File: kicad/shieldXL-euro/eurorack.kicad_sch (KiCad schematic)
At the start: 42 parts, among them J101 Eurorack power, J102 IN L, J103 IN R, J104 OUT L, J105 OUT R, J106 MIDI IN, J107 MIDI OUT, J108 USB-C 5V, J109 USB 1, J110 USB 2, J111 USB 3, J112 Pi USB 1, J113 Pi USB 2, J114 Pi USB 3, U101 TL074

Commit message: Corone schematic, and its jacks and header on the main board
kicad/corone: a generated schematic for the crow daughterboard, for monome's
own firmware - STM32F722RET6, ADS131A02 (symbol from TI's pin table), DAC8565,
OPA4197 output and input stages scaled to the firmware's conversions, ADG1408
calibration mux onto input 1's normal, switched ii pull-ups, USB with VBUS
sense, rack-only power. ERC: three expected warnings, no errors.

eurorack sheet: the six CORONE jacks (I/1's switch contact carried to the
mux), the 2 x 10 header, the ii header and a cable header for the Pi's
fourth USB port. Main-project ERC unchanged at 35.

Co-Authored-By: Claude Opus 5.5 <noreply@anthropic.com>
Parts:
- added J109: USB 1, Connector_USB:USB_A_Molex_105057_Vertical, symbol Connector:USB_A
- added J116: CORONE I/2, MMM:Jack_3.5mm_QingPu_WQP-PJ398SM_Vertical_CircularHoles, symbol Connector_Audio:AudioJack2_SwitchT
- added J117: CORONE O/1, MMM:Jack_3.5mm_QingPu_WQP-PJ398SM_Vertical_CircularHoles, symbol Connector_Audio:AudioJack2_SwitchT
- added J118: CORONE O/2, MMM:Jack_3.5mm_QingPu_WQP-PJ398SM_Vertical_CircularHoles, symbol Connector_Audio:AudioJack2_SwitchT
- added J119: CORONE O/3, MMM:Jack_3.5mm_QingPu_WQP-PJ398SM_Vertical_CircularHoles, symbol Connector_Audio:AudioJack2_SwitchT
- added J120: CORONE O/4, MMM:Jack_3.5mm_QingPu_WQP-PJ398SM_Vertical_CircularHoles, symbol Connector_Audio:AudioJack2_SwitchT
- added J121: Corone, Connector_PinHeader_2.54mm:PinHeader_2x10_P2.54mm_Vertical, symbol Connector_Generic:Conn_02x10_Odd_Even
- added J122: ii, Connector_PinHeader_2.54mm:PinHeader_1x03_P2.54mm_Vertical, symbol Connector_Generic:Conn_01x03
- added J123: Pi USB 4, Connector_JST:JST_PH_B4B-PH-K_1x04_P2.00mm_Vertical, symbol Connector_Generic:Conn_01x04
- J115: renamed from J109; value USB 1 -> CORONE I/1; footprint Connector_USB:USB_A_Molex_105057_Vertical -> MMM:Jack_3.5mm_QingPu_WQP-PJ398SM_Vertical_CircularHoles; symbol Connector:USB_A -> Connector_Audio:AudioJack2_SwitchT
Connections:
- net +12V: now also J121.1 (Pin_1)
- net -12V: now also J121.2 (Pin_2)
- net AGND: now also J115.S, J116.S, J116.TN, J117.S, J118.S, J119.S, J120.S, J121.13 (Pin_13), J121.14 (Pin_14), J121.18 (Pin_18), J121.3 (Pin_3), J121.4 (Pin_4), J121.8 (Pin_8), J122.1 (Pin_1)
- net GND: now also J109.4 (GND), J109.SH (Shield), J123.4 (Pin_4); no longer J115.4 (GND), J115.SH (Shield)
- net USB1_DM: now also J109.2 (D-); no longer J115.2 (D-)
- net USB1_DP: now also J109.3 (D+); no longer J115.3 (D+)
- net USB1_VBUS: now also J109.1 (VBUS); no longer J115.1 (VBUS)
- new net CRW_IN1: J115.T, J121.5 (Pin_5)
- new net CRW_IN1_NORM: J115.TN, J121.6 (Pin_6)
- new net CRW_IN2: J116.T, J121.7 (Pin_7)
- new net CRW_OUT1: J117.T, J121.9 (Pin_9)
- new net CRW_OUT2: J118.T, J121.10 (Pin_10)
- new net CRW_OUT3: J119.T, J121.11 (Pin_11)
- new net CRW_OUT4: J120.T, J121.12 (Pin_12)
- new net CRW_USB_DM: J121.16 (Pin_16), J123.2 (Pin_2)
- new net CRW_USB_DP: J121.15 (Pin_15), J123.3 (Pin_3)
- new net CRW_VBUS: J121.17 (Pin_17), J123.1 (Pin_1)
- new net II_SCL: J121.19 (Pin_19), J122.2 (Pin_2)
- new net II_SDA: J121.20 (Pin_20), J122.3 (Pin_3)
- no-connect marks 3 -> 7

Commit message: Pi USB adapter, and the main board's two IDC headers for it
kicad/usb-adapter: a generated board that stands at one of the Pi 4's USB
stacks, two vertical male USB-A plugs in its ports and a 2 x 5 IDC whose
ribbon runs behind the Pi to the main board; two identical boards cover the
four ports. The plug footprint and the port spacing are placeholders until
the part is chosen and the Pi measured. Unrouted.

eurorack sheet: J112 / J113, 2 x 5 IDC, replace the four JST cable headers;
Corone's USB comes from J113's port B. ERC unchanged at 35.

Co-Authored-By: Claude Opus 5.5 <noreply@anthropic.com>
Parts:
- removed J109: USB 1, Connector_USB:USB_A_Molex_105057_Vertical, symbol Connector:USB_A
- removed J112: Pi USB 1, Connector_JST:JST_PH_B4B-PH-K_1x04_P2.00mm_Vertical, symbol Connector_Generic:Conn_01x04
- removed J113: Pi USB 2, Connector_JST:JST_PH_B4B-PH-K_1x04_P2.00mm_Vertical, symbol Connector_Generic:Conn_01x04
- removed J114: Pi USB 3, Connector_JST:JST_PH_B4B-PH-K_1x04_P2.00mm_Vertical, symbol Connector_Generic:Conn_01x04
- added J112: Pi USB, inner stack, Connector_IDC:IDC-Header_2x05_P2.54mm_Vertical, symbol Connector_Generic:Conn_02x05_Odd_Even
- added J113: Pi USB, outer stack, Connector_IDC:IDC-Header_2x05_P2.54mm_Vertical, symbol Connector_Generic:Conn_02x05_Odd_Even
- J109: renamed from J123; value Pi USB 4 -> USB 1; footprint Connector_JST:JST_PH_B4B-PH-K_1x04_P2.00mm_Vertical -> Connector_USB:USB_A_Molex_105057_Vertical; symbol Connector_Generic:Conn_01x04 -> Connector:USB_A
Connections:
- net CRW_USB_DM: now also J113.7 (Pin_7); no longer J109.2 (Pin_2)
- net CRW_USB_DP: now also J113.8 (Pin_8); no longer J109.3 (Pin_3)
- net GND: now also J109.SH (Shield), J112.2 (Pin_2), J112.5 (Pin_5), J112.6 (Pin_6), J112.9 (Pin_9), J113.2 (Pin_2), J113.5 (Pin_5), J113.6 (Pin_6), J113.9 (Pin_9)
- net USB1_DM: now also J109.2 (D-), J112.3 (Pin_3)
- net USB1_DP: now also J109.3 (D+), J112.4 (Pin_4)
- net USB1_VBUS: now also J109.1 (VBUS), J112.1 (Pin_1)
- net USB2_DM: now also J112.7 (Pin_7)
- net USB2_DP: now also J112.8 (Pin_8)
- net USB2_VBUS: now also J112.10 (Pin_10)
- net USB3_DM: now also J113.3 (Pin_3)
- net USB3_DP: now also J113.4 (Pin_4)
- net USB3_VBUS: now also J113.1 (Pin_1)
- net CRW_VBUS renamed CRW_USB_VBUS
- net CRW_USB_VBUS: now also J113.10 (Pin_10); no longer J109.1 (Pin_1)

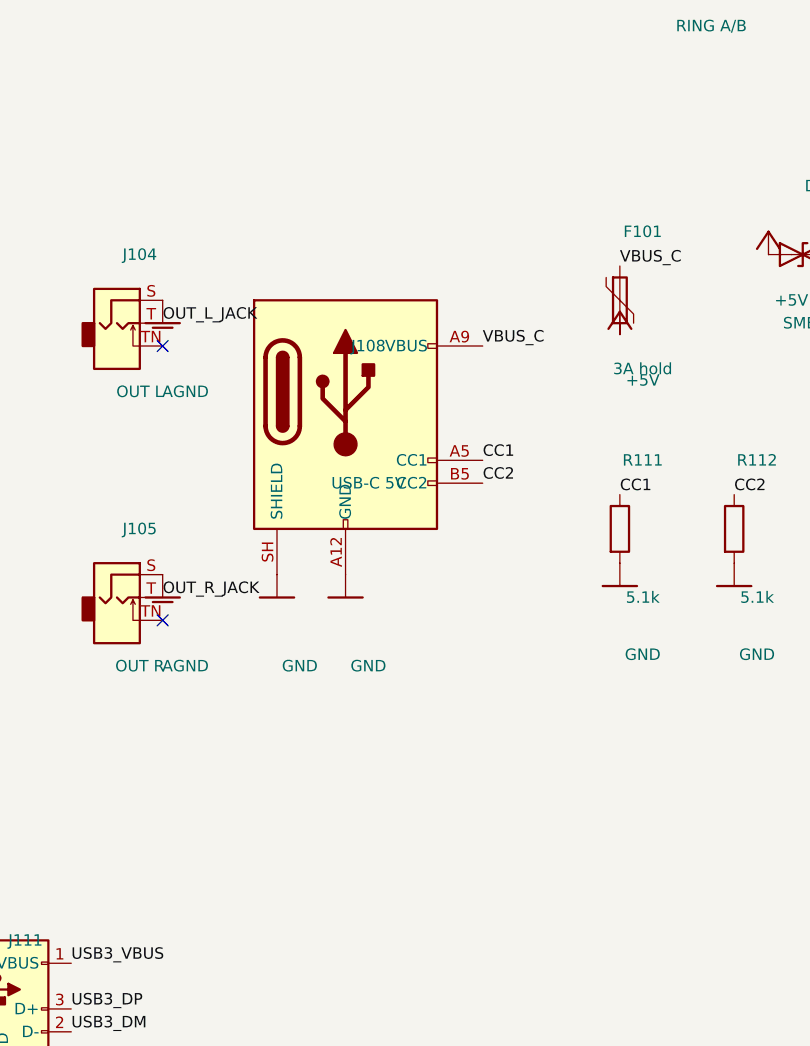
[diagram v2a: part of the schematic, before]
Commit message: USB-C power: Molex 204711-0001 vertical receptacle; display holes
J108 gets a footprint from Molex's recommended PCB layout (drawing
2047110001 sheet 3) and the full 24-contact symbol, so all four VBUS and
four GND contacts carry current; CC1 / CC2 keep their 5.1k, the data pins
are left open. make_outline.py drills three of the display module's four
holes (d2.5); the top-left one falls on the Pi header's pin 2.

Co-Authored-By: Claude Opus 5.5 <noreply@anthropic.com>
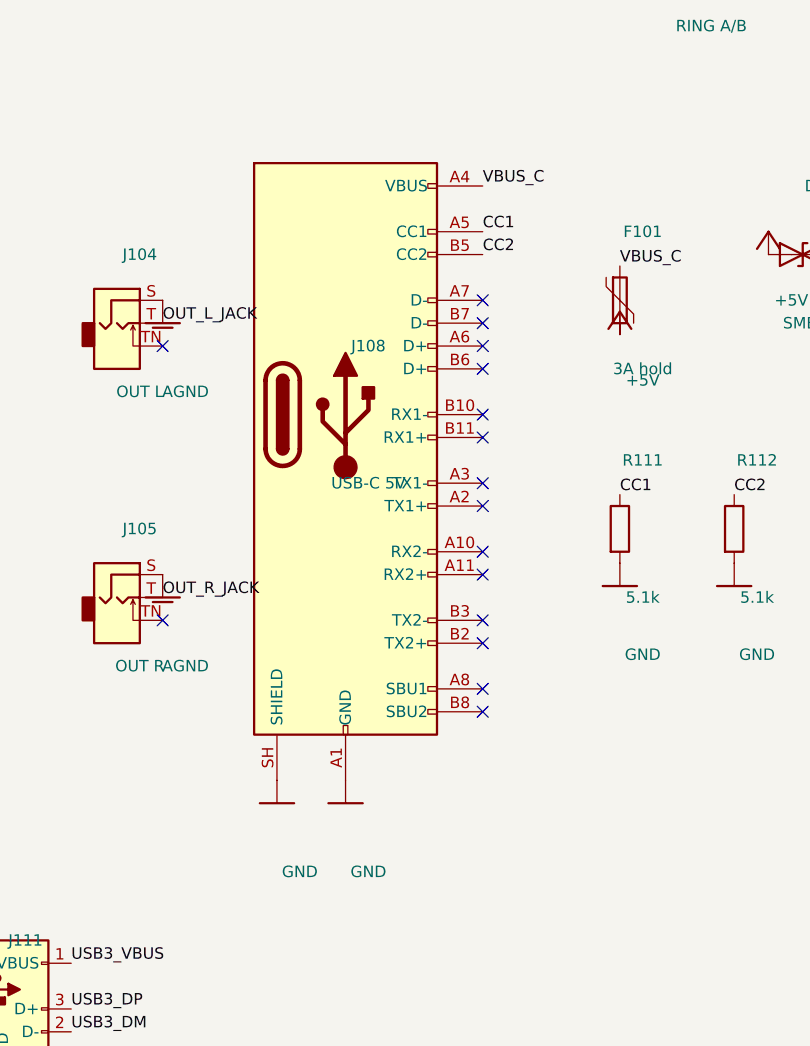
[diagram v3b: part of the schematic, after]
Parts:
- removed C113: 47u, Capacitor_SMD:C_1206_3216Metric, symbol Device:C
- removed J117: CORONE O/1, MMM:Jack_3.5mm_QingPu_WQP-PJ398SM_Vertical_CircularHoles, symbol Connector_Audio:AudioJack2_SwitchT
- removed R111: 5.1k, Resistor_SMD:R_0805_2012Metric, symbol Device:R
- added J115: CORONE I/1, MMM:Jack_3.5mm_QingPu_WQP-PJ398SM_Vertical_CircularHoles, symbol Connector_Audio:AudioJack2_SwitchT
- added J118: CORONE O/2, MMM:Jack_3.5mm_QingPu_WQP-PJ398SM_Vertical_CircularHoles, symbol Connector_Audio:AudioJack2_SwitchT
- added J121: Corone, Connector_PinHeader_2.54mm:PinHeader_2x10_P2.54mm_Vertical, symbol Connector_Generic:Conn_02x10_Odd_Even
- C113: renamed from J118; value CORONE O/2 -> 47u; footprint MMM:Jack_3.5mm_QingPu_WQP-PJ398SM_Vertical_CircularHoles -> Capacitor_SMD:C_1206_3216Metric; symbol Connector_Audio:AudioJack2_SwitchT -> Device:C
- J108: footprint (none) -> MMM:USB_C_Receptacle_Molex_2047110001_Vertical; symbol Connector:USB_C_Receptacle_PowerOnly_6P -> Connector:USB_C_Receptacle
- J117: renamed from J121; value Corone -> CORONE O/1; footprint Connector_PinHeader_2.54mm:PinHeader_2x10_P2.54mm_Vertical -> MMM:Jack_3.5mm_QingPu_WQP-PJ398SM_Vertical_CircularHoles; symbol Connector_Generic:Conn_02x10_Odd_Even -> Connector_Audio:AudioJack2_SwitchT
- R111: renamed from J115; value CORONE I/1 -> 5.1k; footprint MMM:Jack_3.5mm_QingPu_WQP-PJ398SM_Vertical_CircularHoles -> Resistor_SMD:R_0805_2012Metric; symbol Connector_Audio:AudioJack2_SwitchT -> Device:R
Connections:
- net +12V: now also J121.1 (Pin_1); no longer J117.1 (Pin_1)
- net +5V: now also C113.1
- net -12V: now also J121.2 (Pin_2); no longer J117.2 (Pin_2)
- net AGND: now also J117.S, J115.S, J118.S, J121.13 (Pin_13), J121.14 (Pin_14), J121.18 (Pin_18), J121.3 (Pin_3), J121.4 (Pin_4), J121.8 (Pin_8); no longer C113.S, J117.13 (Pin_13), J117.14 (Pin_14), J117.18 (Pin_18), J117.3 (Pin_3), J117.4 (Pin_4), J117.8 (Pin_8), R111.S
- net CC1: now also R111.1
- net CRW_IN1: now also J115.T, J121.5 (Pin_5); no longer J117.5 (Pin_5), R111.T
- net CRW_IN1_NORM: now also J115.TN, J121.6 (Pin_6); no longer J117.6 (Pin_6), R111.TN
- net CRW_IN2: now also J121.7 (Pin_7); no longer J117.7 (Pin_7)
- net CRW_OUT1: now also J117.T, J121.9 (Pin_9); no longer J117.9 (Pin_9)
- net CRW_OUT2: now also J118.T, J121.10 (Pin_10); no longer C113.T, J117.10 (Pin_10)
- net CRW_OUT3: now also J121.11 (Pin_11); no longer J117.11 (Pin_11)
- net CRW_OUT4: now also J121.12 (Pin_12); no longer J117.12 (Pin_12)
- net CRW_USB_DM: now also J121.16 (Pin_16); no longer J117.16 (Pin_16)
- net CRW_USB_DP: now also J121.15 (Pin_15); no longer J117.15 (Pin_15)
- net CRW_USB_VBUS: now also J121.17 (Pin_17); no longer J117.17 (Pin_17)
- net GND: now also C113.2, J108.A1 (GND), J108.B1 (GND), R111.2
- net II_SCL: now also J121.19 (Pin_19); no longer J117.19 (Pin_19)
- net II_SDA: now also J121.20 (Pin_20); no longer J117.20 (Pin_20)
- net VBUS_C: now also J108.A4 (VBUS), J108.B4 (VBUS)
- no-connect marks 7 -> 21
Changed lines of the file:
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@@
 	)
 	(symbol
-		(lib_id "Connector:USB_C_Receptacle_PowerOnly_6P")
+		(lib_id "Connector:USB_C_Receptacle")
 		(at 241.3 116.84 0)
 		(unit 1)
@@
 			)
 		)
-		(property "Footprint" ""
+		(property "Footprint" "MMM:USB_C_Receptacle_Molex_2047110001_Vertical"
 			(at 241.3 116.84 0)
 			(hide yes)
@@
 			)
 		)
+		(pin "A1"
+		)
+		(pin "A2"
+		)
+		(pin "A3"
+		)
+		(pin "A4"
+		)
 		(pin "A5"
 		)
+		(pin "A6"
+		)
+		(pin "A7"
+		)
+		(pin "A8"
+		)
 		(pin "A9"
 		)
+		(pin "A10"
+		)
+		(pin "A11"
+		)
 		(pin "A12"
 		)
+		(pin "B1"
+		)
+		(pin "B2"
+		)
+		(pin "B3"
+		)
+		(pin "B4"
+		)
 		(pin "B5"
 		)
+		(pin "B6"
+		)
+		(pin "B7"
+		)
+		(pin "B8"
+		)
 		(pin "B9"
+		)
+		(pin "B10"
+		)
+		(pin "B11"
 		)
 		(pin "B12"
@@
 	)
 	(label "VBUS_C"
-		(at 256.54 109.22 0)
+		(at 256.54 91.44 0)
 		(effects
 			(font
@@
 	(symbol
 		(lib_id "norns-shield-210330-eagle-import:GND")
-		(at 241.3 137.16 0)
+		(at 241.3 160.02 0)
 		(unit 1)
 		(exclude_from_sim no)
@@
 		(dnp no)
 		(property "Reference" "#PWR130"
-			(at 243.84 129.54 0)
+			(at 243.84 152.4 0)
 			(hide yes)
 			(effects
@@
 		)
 		(property "Value" "GND"
-			(at 243.84 144.78 0)
+			(at 243.84 167.64 0)
 			(effects
 				(font
@@
 		)
 		(property "Footprint" ""
-			(at 241.3 137.16 0)
+			(at 241.3 160.02 0)
 			(hide yes)
 			(effects
@@
 		)
 		(property "Datasheet" ""
-			(at 241.3 137.16 0)
+			(at 241.3 160.02 0)
 			(hide yes)
 			(effects
@@
 		)
 	)
-	(label "CC1"
-		(at 256.54 121.92 0)
-		(effects
-			(font
-				(size 1.27 1.27)
-			)
-			(justify left bottom)
-		)
-	)
-	(label "CC2"
-		(at 256.54 124.46 0)
-		(effects
-			(font
-				(size 1.27 1.27)
-			)
-			(justify left bottom)
-		)
-	)
 	(symbol
 		(lib_id "norns-shield-210330-eagle-import:GND")
-		(at 233.68 137.16 0)
+		(at 233.68 160.02 0)
 		(unit 1)
 		(exclude_from_sim no)
@@
 		(dnp no)
 		(property "Reference" "#PWR131"
-			(at 236.22 129.54 0)
+			(at 236.22 152.4 0)
 			(hide yes)
 			(effects
@@
 		)
 		(property "Value" "GND"
-			(at 236.22 144.78 0)
+			(at 236.22 167.64 0)
 			(effects
 				(font
@@
 		)
 		(property "Footprint" ""
-			(at 233.68 137.16 0)
+			(at 233.68 160.02 0)
 			(hide yes)
 			(effects
@@
 		)
 		(property "Datasheet" ""
-			(at 233.68 137.16 0)
+			(at 233.68 160.02 0)
 			(hide yes)
 			(effects
@@
 		)
 	)
-	(symbol
+	(label "CC1"
+		(at 256.54 96.52 0)
+		(effects
+			(font
+				(size 1.27 1.27)
+			)
+			(justify left bottom)
+		)
+	)
+	(label "CC2"
+		(at 256.54 99.06 0)
+		(effects
+			(font
+				(size 1.27 1.27)
+			)
+			(justify left bottom)
+		)
+	)
+	(no_connect
+		(at 256.54 127)
+	)
+	(no_connect
+		(at 256.54 124.46)
+	)
+	(no_connect
+		(at 256.54 109.22)
+	)
+	(no_connect
+		(at 256.54 104.14)
+	)
+	(no_connect
+		(at 256.54 147.32)
+	)
+	(no_connect
+		(at 256.54 132.08)
+	)
+	(no_connect
+		(at 256.54 134.62)
+	)
+	(no_connect
+		(at 256.54 142.24)
+	)
+	(no_connect
+		(at 256.54 139.7)
+	)
+	(no_connect
+		(at 256.54 111.76)
+	)
+	(no_connect
+		(at 256.54 106.68)
+	)
+	(no_connect
+		(at 256.54 149.86)
+	)
+	(no_connect
+		(at 256.54 116.84)
+	)
+	(no_connect
+		(at 256.54 119.38)
+	)
+	(symbol

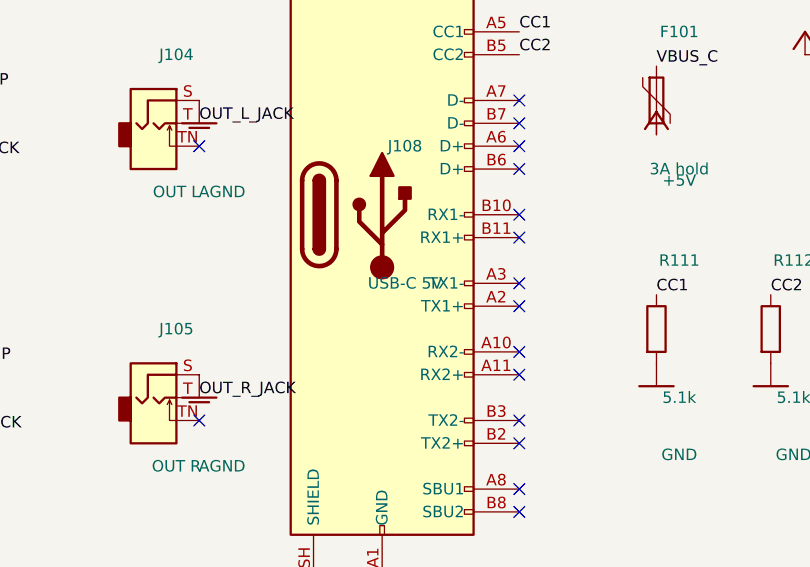
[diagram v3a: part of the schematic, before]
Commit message: J108 to the 12 mm JAE DX07S024WJ1R350; the display in 3D
The Molex 204711 stood 9.05 mm, about 2.5 mm short of letting a plug seat
through the panel. The JAE high-profile receptacle stands 12.0 mm, its face
about at the panel's front; KiCad's footprint has the same pin names, so J108
swapped in place with its nets. Its 3D model is still to come.

DS1 is a board-only footprint for the NHD-2.7-12864WDW3 module (outline,
holes and viewing area on F.Fab, origin at its top-left), placed by
place_panel_parts.py, carrying Newhaven's 3D model with the glass 9.8 mm up,
just behind the panel. The model is the CTP variant: same module, plus a
touch panel and its flex tail, which the -M module does not have.

Co-Authored-By: Claude Opus 5.5 <noreply@anthropic.com>
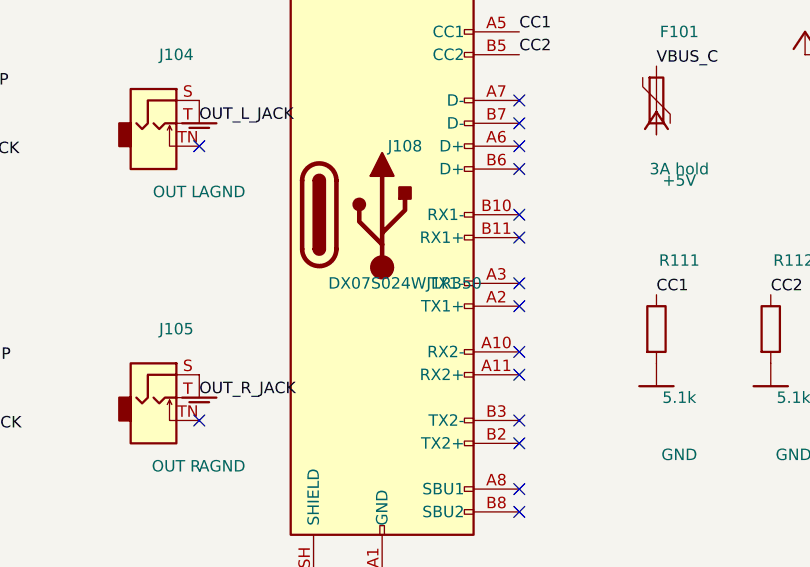
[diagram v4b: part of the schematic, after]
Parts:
- J108: value USB-C 5V -> DX07S024WJ1R350; footprint MMM:USB_C_Receptacle_Molex_2047110001_Vertical -> Connector_USB:USB_C_Receptacle_JAE_DX07S024WJ1R350
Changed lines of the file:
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@@
 			)
 		)
-		(property "Value" "USB-C 5V"
+		(property "Value" "DX07S024WJ1R350"
 			(at 243.84 124.46 0)
 			(effects
@@
 			)
 		)
-		(property "Footprint" "MMM:USB_C_Receptacle_Molex_2047110001_Vertical"
+		(property "Footprint" "Connector_USB:USB_C_Receptacle_JAE_DX07S024WJ1R350"
 			(at 241.3 116.84 0)
 			(hide yes)
